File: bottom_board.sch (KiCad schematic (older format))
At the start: 15 parts, among them J201 VAC, J202 Conn_01x03_Female, K201 SANYOU_SRD_Form_C, Q201 Q_NPN

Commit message: Start defining PCB
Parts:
- J202: footprint (none) -> Connector_PinHeader_2.54mm:PinHeader_1x03_P2.54mm_Vertical
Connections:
- net C: now also J201.1 (Pin_1); no longer J201.2 (Pin_2)
- net NC: now also J201.2 (Pin_2); no longer J201.3 (Pin_3)
- net NO: now also J201.3 (Pin_3); no longer J201.1 (Pin_1)
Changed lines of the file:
@@
 Text Label 10000 1600 0    50   ~ 0
 C
-Text Label 1650 1550 0    50   ~ 0
+Text Label 1650 1750 0    50   ~ 0
 NO
-Text Label 1650 1750 0    50   ~ 0
+Text Label 1650 1650 0    50   ~ 0
 NC
 $Comp
@@
 Wire Wire Line
 	1650 1550 1800 1550
-Text Label 1650 1650 0    50   ~ 0
+Text Label 1650 1550 0    50   ~ 0
 C
 Text Label 1650 1950 0    50   ~ 0
@@
 F 0 "J202" H 2128 3126 50  0000 L CNN
 F 1 "Conn_01x03_Female" H 2128 3035 50  0000 L CNN
-F 2 "" H 2100 3100 50  0001 C CNN
+F 2 "Connector_PinHeader_2.54mm:PinHeader_1x03_P2.54mm_Vertical" H 2100 3100 50  0001 C CNN
 F 3 "~" H 2100 3100 50  0001 C CNN
 	1    2100 3100

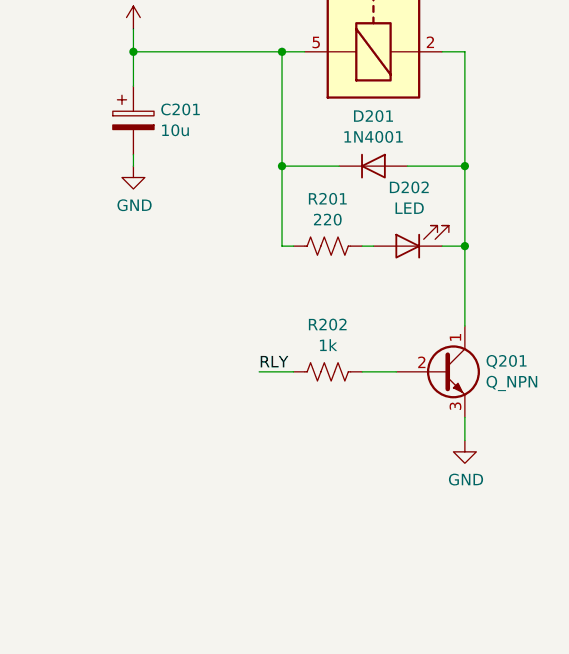
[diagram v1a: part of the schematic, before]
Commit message: Fix minor PCB mistakes and bump up the version to 1.01
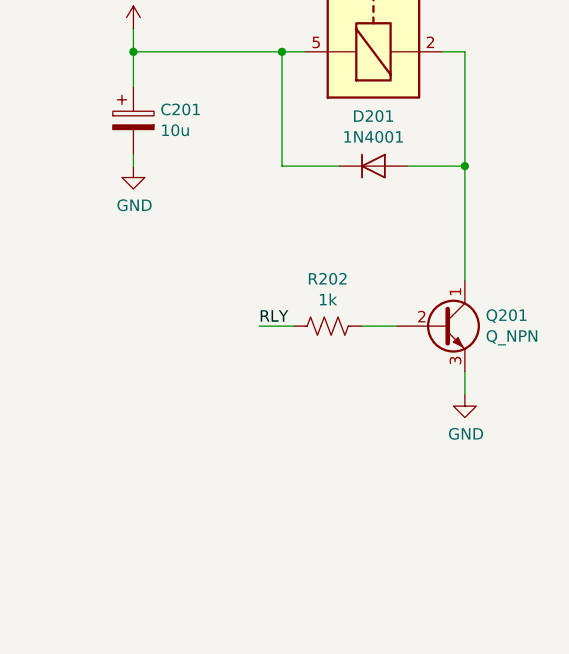
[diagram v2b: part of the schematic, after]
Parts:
- removed D202: LED, LED_THT:LED_D3.0mm, symbol Device:LED
- removed R201: 220, Resistor_THT:R_Axial_DIN0207_L6.3mm_D2.5mm_P7.62mm_Horizontal, symbol Device:R_US
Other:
- moved on the sheet: Q201, R202
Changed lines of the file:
@@
 L Device:Q_NPN_CBE Q?
 U 1 1 60923639
-P 9900 3400
+P 9900 3200
 AR Path="/60923639" Ref="Q?"  Part="1"
 AR Path="/5FC173C3/60923639" Ref="Q201"  Part="1"
-F 0 "Q201" H 10091 3446 50  0000 L CNN
-F 1 "Q_NPN" H 10091 3355 50  0000 L CNN
-F 2 "Package_TO_SOT_THT:TO-92L_Inline_Wide" H 10100 3500 50  0001 C CNN
-F 3 "~" H 9900 3400 50  0001 C CNN
-	1    9900 3400
+F 0 "Q201" H 10091 3246 50  0000 L CNN
+F 1 "Q_NPN" H 10091 3155 50  0000 L CNN
+F 2 "Package_TO_SOT_THT:TO-92L_Inline_Wide" H 10100 3300 50  0001 C CNN
+F 3 "~" H 9900 3200 50  0001 C CNN
+	1    9900 3200
 	1    0    0    -1
 $EndComp
@@
 L power:GND #PWR?
 U 1 1 6092363F
-P 10000 3700
+P 10000 3500
 AR Path="/6092363F" Ref="#PWR?"  Part="1"
 AR Path="/5FC173C3/6092363F" Ref="#PWR0207"  Part="1"
-F 0 "#PWR0207" H 10000 3450 50  0001 C CNN
-F 1 "GND" H 10005 3527 50  0000 C CNN
-F 2 "" H 10000 3700 50  0001 C CNN
-F 3 "" H 10000 3700 50  0001 C CNN
-	1    10000 3700
+F 0 "#PWR0207" H 10000 3250 50  0001 C CNN
+F 1 "GND" H 10005 3327 50  0000 C CNN
+F 2 "" H 10000 3500 50  0001 C CNN
+F 3 "" H 10000 3500 50  0001 C CNN
+	1    10000 3500
 	1    0    0    -1
 $EndComp
@@
 	9900 2000 10000 2000
 Wire Wire Line
-	10000 2000 10000 2500
-Wire Wire Line
-	10000 3600 10000 3700
+	10000 3400 10000 3500
 $Comp
 L Device:R_US R?
 U 1 1 60923648
-P 9400 3400
+P 9400 3200
 AR Path="/60923648" Ref="R?"  Part="1"
 AR Path="/5FC173C3/60923648" Ref="R202"  Part="1"
-F 0 "R202" V 9195 3400 50  0000 C CNN
-F 1 "1k" V 9286 3400 50  0000 C CNN
-F 2 "Resistor_THT:R_Axial_DIN0207_L6.3mm_D2.5mm_P7.62mm_Horizontal" V 9440 3390 50  0001 C CNN
-F 3 "~" H 9400 3400 50  0001 C CNN
-	1    9400 3400
+F 0 "R202" V 9195 3200 50  0000 C CNN
+F 1 "1k" V 9286 3200 50  0000 C CNN
+F 2 "Resistor_THT:R_Axial_DIN0207_L6.3mm_D2.5mm_P7.62mm_Horizontal" V 9440 3190 50  0001 C CNN
+F 3 "~" H 9400 3200 50  0001 C CNN
+	1    9400 3200
 	0    1    1    0
 $EndComp
 Wire Wire Line
-	9250 3400 9100 3400
-Wire Wire Line
-	9550 3400 9700 3400
-Text Label 9100 3400 0    50   ~ 0
+	9250 3200 9100 3200
+Wire Wire Line
+	9550 3200 9700 3200
+Text Label 9100 3200 0    50   ~ 0
 RLY
 $Comp
@@
 Wire Wire Line
 	8550 2000 9200 2000
-$Comp
-L Device:LED D?
-U 1 1 60923677
-P 9750 2850
-AR Path="/60923677" Ref="D?"  Part="1"
-AR Path="/5FC173C3/60923677" Ref="D202"  Part="1"
-F 0 "D202" H 9743 2595 50  0000 C CNN
-F 1 "LED" H 9743 2686 50  0000 C CNN
-F 2 "LED_THT:LED_D3.0mm" H 9750 2850 50  0001 C CNN
-F 3 "~" H 9750 2850 50  0001 C CNN
-	1    9750 2850
-	-1   0    0    1
-$EndComp
-$Comp
-L Device:R_US R?
-U 1 1 6092367D
-P 9400 2850
-AR Path="/6092367D" Ref="R?"  Part="1"
-AR Path="/5FC173C3/6092367D" Ref="R201"  Part="1"
-F 0 "R201" V 9195 2850 50  0000 C CNN
-F 1 "220" V 9286 2850 50  0000 C CNN
-F 2 "Resistor_THT:R_Axial_DIN0207_L6.3mm_D2.5mm_P7.62mm_Horizontal" V 9440 2840 50  0001 C CNN
-F 3 "~" H 9400 2850 50  0001 C CNN
-	1    9400 2850
-	0    1    1    0
-$EndComp
-Wire Wire Line
-	9200 2500 9200 2850
-Wire Wire Line
-	9200 2850 9250 2850
-Connection ~ 9200 2500
-Wire Wire Line
-	9550 2850 9600 2850
-Wire Wire Line
-	10000 2500 10000 2850
 Connection ~ 10000 2500
-Wire Wire Line
-	9900 2850 10000 2850
-Connection ~ 10000 2850
-Wire Wire Line
-	10000 2850 10000 3200
 Wire Wire Line
 	1650 1650 1800 1650
@@
 Text Label 5900 4650 2    50   ~ 0
 RLY
+Wire Wire Line
+	10000 2500 10000 3000
+Wire Wire Line
+	10000 2000 10000 2500
 $EndSCHEMATC
